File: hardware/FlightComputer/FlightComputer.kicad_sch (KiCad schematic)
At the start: 46 parts

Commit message: Add USB, Sensor Stack, Camera, TestPoints.
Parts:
- removed C? (x3): Capacitor 10nF +/-20% 50V 0402, CAPC0402(1005)60_L, symbol FCU-altium-import:0_CAP-NP-2
- removed C?: Capacitor 10nF +/-20% 50V 0402, CAPC0402(1005)60_L, symbol FCU-altium-import:2_CAP-NP-2
- removed C?: Capacitor 1µF +/-0.1% 25V 0603, CAPC0603(1608)100_L, symbol FCU-altium-import:3_CAP-NP-2
- removed C? (x2): Capacitor, symbol FCU-altium-import:1_Capacitor
- added C? (x2): 10n, symbol Device:C_Small
- added C? (x2): 22n, symbol Device:C_Small
- added C? (x2): 100n, symbol Device:C_Small
- added C?: 1u, symbol Device:C_Small
- added J?: Mag, Connector_PinSocket_2.54mm:PinSocket_1x09_P2.54mm_Vertical, symbol Connector:Conn_01x09_Female
- added J?: Camera, symbol Connector:Conn_01x08_Female
- added J?: IMU, symbol Connector:Conn_01x05_Female
- added J?: USB_B_Micro, symbol Connector:USB_B_Micro
- added R? (x3): 4k7, symbol Device:R_Small
- added R? (x2): 20, symbol Device:R_Small
- added TP? (x15): TestPoint, symbol Connector:TestPoint
- added U? (x3): LM75AD, symbol LM75A:SO8
- added U?: USBLC6-2SC6, Package_TO_SOT_SMD:SOT-23-6, symbol Power_Protection:USBLC6-2SC6
- J?: value Conn_02x05_Odd_Even -> SWD
- R?: ALTIUM_VALUE 162K -> 162k
- R?: value pick one -> 1k
- R?: ALTIUM_VALUE 133K -> 133k
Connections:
- net +3V3: now also R?.1, R?.1, TP?.1
- net +5V: now also C?.1, C?.1, TP?.1
- net EN1: now also TP?.1
- net EN2: now also TP?.1
- net GND: now also C?.2, C?.2, C?.2, J?.2 (Pin_2), J?.2 (Pin_2), J?.4 (ID), J?.5 (GND), J?.5 (Pin_5), J?.7 (Pin_7), TP?.1, U?.2 (GND), U?.4 (GND), U?.4 (GND), U?.4 (GND), U?.5 (A2), U?.5 (A2), U?.6 (A1)
- net GNDA: now also C?.1, C?.2, TP?.1
- net I2C1_SCL: now also R?.2, J?.4 (Pin_4), J?.8 (Pin_8), TP?.1, U?.2 (SCL), U?.2 (SCL), U?.2 (SCL); no longer R?.2
- net I2C1_SDA: now also R?.2, J?.3 (Pin_3), J?.7 (Pin_7), TP?.1, U?.1 (SDA), U?.1 (SDA), U?.1 (SDA); no longer R?.2
- net I2C2_SCL: now also R?.2, TP?.1
- net I2C2_SDA: now also R?.2, TP?.1
- net LED_STATUS: now also U?.51 (PB12); no longer U?.46 (PE15)
- net SPI1_MISO: now also J?.3 (Pin_3), J?.5 (Pin_5), TP?.1
- net SPI1_MOSI: now also J?.2 (Pin_2), J?.4 (Pin_4), TP?.1
- net SPI1_SCK: now also J?.3 (Pin_3), J?.4 (Pin_4), TP?.1
- net USB_D+: now also U?.4 (I/O2)
- net USB_D-: now also U?.6 (I/O1)
- net at IC?.15 (VBST2): now also C?.1
- net at IC?.14 (SW2), L?.1: now also C?.2
- net at IC?.6 (SS1): now also C?.2
- net at IC?.2 (VBST1): now also C?.2
- net at IC?.3 (SW1), L?.2: now also C?.1
- net at IC?.9 (VREG5): now also C?.1
- net CS2: now reaches U?.23 (PA0)
- net CS2: now also J?.6 (Pin_6), TP?.1
- net CS1: now reaches U?.67 (PA8)
- net CS1: now also J?.1 (Pin_1), TP?.1
- net at IC?.11 (SS2): now also C?.1
- new net: J?.3 (D+), R?.1, R?.2
- new net: J?.2 (D-), R?.2
- new net +3.3V: J?.1 (Pin_1), J?.1 (Pin_1), J?.6 (Pin_6), U?.5 (A2), U?.6 (A1), U?.6 (A1), U?.7 (A0), U?.7 (A0), U?.7 (A0), U?.8 (VCC), U?.8 (VCC), U?.8 (VCC)
- new net +5VD: J?.1 (VBUS), R?.1, U?.5 (VBUS)
- new net PE15: U?.46 (PE15)
- new net USB_CONN_D+: R?.2, U?.3 (I/O2)
- new net USB_CONN_D-: R?.1, U?.1 (I/O1)
- no-connect marks 2 -> 9
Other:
- note added: "I2C Devices"
- note added: "Power Conditioning"
- note added: "Rail Creation"
- note added: "SPI Devices"
- note added: "Serial Wire Debug"
- note added: "USB"
- note added: "X OSC"
- moved on the sheet: C?, D?, J?, L?, R?, SW?, U?, Y?

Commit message: Add Annotations
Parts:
- gave numbers to parts that had none: 74

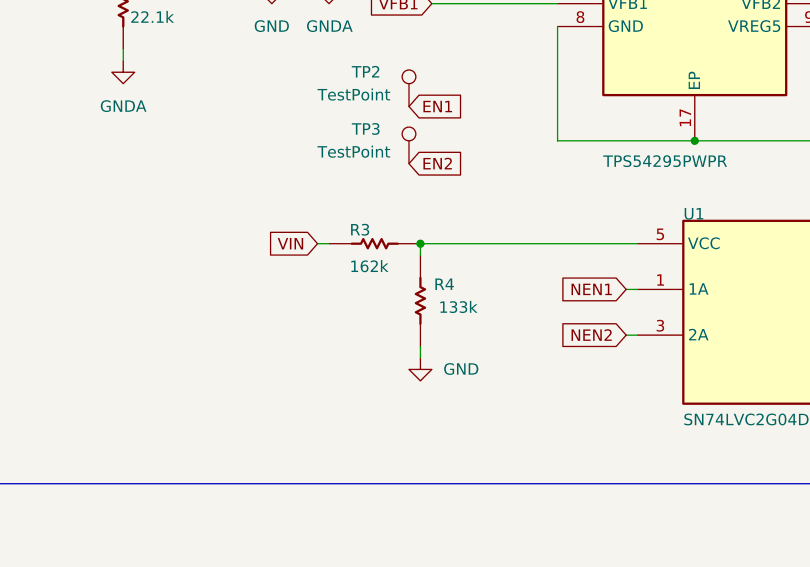
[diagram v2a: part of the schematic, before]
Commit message: Migrate some altium stuff to KiCad version
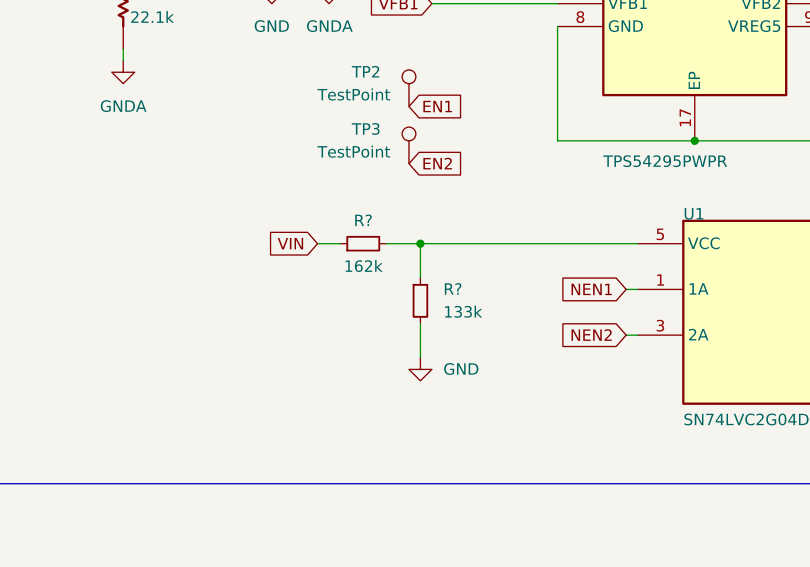
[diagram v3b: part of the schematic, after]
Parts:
- removed R3: Resistor, symbol FCU-altium-import:2_Resistor
- removed R4: Resistor, symbol FCU-altium-import:3_Resistor
- added R?: 133k, symbol Device:R_Small
- added R?: 162k, symbol Device:R_Small
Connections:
- net GND: now also R?.2
- net VIN: now also R?.1
- net at U1.5 (VCC): now also R?.1, R?.2
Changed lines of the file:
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@@
   (junction (at 379.73 119.38) (diameter 0) (color 0 0 0 0)
   )
-  (junction (at 73.66 120.65) (diameter 0) (color 0 0 0 0)
-  )
   (junction (at 156.21 76.2) (diameter 0) (color 0 0 0 0)
   )
@@
   (junction (at 379.73 116.84) (diameter 0) (color 0 0 0 0)
   )
-  (junction (at 254 76.2) (diameter 0) (color 0 0 0 0)
-  )
   (junction (at 40.64 76.2) (diameter 0) (color 0 0 0 0)
   )
+  (junction (at 254 76.2) (diameter 0) (color 0 0 0 0)
+  )
   (junction (at 379.73 157.48) (diameter 0) (color 0 0 0 0)
   )
@@
   (junction (at 152.4 76.2) (diameter 0) (color 0 0 0 0)
   )
+  (junction (at 73.66 120.65) (diameter 0) (color 0 0 0 0)
+  )
   (junction (at 88.9 68.58) (diameter 0) (color 0 0 0 0)
   )
@@
     (stroke (width 0) (type default) (color 0 0 0 0))
   )
-  (wire (pts (xy 62.23 120.65) (xy 63.5 120.65))
+  (wire (pts (xy 62.23 120.65) (xy 64.77 120.65))
     (stroke (width 0) (type default) (color 0 0 0 0))
   )
@@
     (stroke (width 0) (type default) (color 0 0 0 0))
   )
+  (wire (pts (xy 254 76.2) (xy 256.54 76.2))
+    (stroke (width 0) (type default) (color 0 0 0 0))
+  )
   (wire (pts (xy 328.93 187.96) (xy 328.93 193.04))
     (stroke (width 0) (type default) (color 0 0 0 0))
@@
     (stroke (width 0) (type default) (color 0 0 0 0))
   )
-  (wire (pts (xy 73.66 133.35) (xy 73.66 132.08))
+  (wire (pts (xy 73.66 129.54) (xy 73.66 133.35))
     (stroke (width 0) (type default) (color 0 0 0 0))
   )
@@
     (stroke (width 0) (type default) (color 0 0 0 0))
   )
-  (wire (pts (xy 73.66 121.92) (xy 73.66 120.65))
+  (wire (pts (xy 73.66 120.65) (xy 73.66 124.46))
     (stroke (width 0) (type default) (color 0 0 0 0))
   )
@@
     (stroke (width 0) (type default) (color 0 0 0 0))
   )
+  (wire (pts (xy 69.85 120.65) (xy 73.66 120.65))
+    (stroke (width 0) (type default) (color 0 0 0 0))
+  )
   (wire (pts (xy 166.37 86.36) (xy 166.37 88.9))
     (stroke (width 0.254) (type default) (color 0 0 0 0))
@@
     (stroke (width 0.254) (type default) (color 0 0 0 0))
   )
-  (wire (pts (xy 254 76.2) (xy 256.54 76.2))
-    (stroke (width 0) (type default) (color 0 0 0 0))
-  )
   (wire (pts (xy 323.85 111.76) (xy 330.2 111.76))
     (stroke (width 0) (type default) (color 0 0 0 0))
@@
     (pin "2")
   )
-  (symbol (lib_id "FCU-altium-import:2_Resistor") (at 73.66 120.65 0) (unit 1)
-    (in_bom yes) (on_board yes)
-    (property "Reference" "R3" (id 0) (at 65.786 119.888 0)
-      (effects (font (size 1.27 1.27)) (justify left bottom))
-    )
-    (property "Value" "Resistor" (id 1) (at 62.992 119.888 0)
-      (effects (font (size 1.27 1.27)) (justify left bottom) hide)
-    )
-    (property "Footprint" "" (id 2) (at 73.66 120.65 0)
-      (effects (font (size 1.27 1.27)) hide)
-    )
-    (property "Datasheet" "" (id 3) (at 73.66 120.65 0)
-      (effects (font (size 1.27 1.27)) hide)
-    )
-    (property "DTEMP" "" (id 4) (at 62.992 119.888 0)
-      (effects (font (size 1.27 1.27)) (justify left bottom) hide)
-    )
-    (property "T_REL_LOCAL" "" (id 5) (at 62.992 119.888 0)
-      (effects (font (size 1.27 1.27)) (justify left bottom) hide)
-    )
-    (property "TC" "" (id 6) (at 62.992 119.888 0)
-      (effects (font (size 1.27 1.27)) (justify left bottom) hide)
-    )
-    (property "TC1" "0" (id 7) (at 62.992 119.888 0)
-      (effects (font (size 1.27 1.27)) (justify left bottom) hide)
-    )
-    (property "TC2" "0" (id 8) (at 62.992 119.888 0)
-      (effects (font (size 1.27 1.27)) (justify left bottom) hide)
-    )
-    (property "TEMP" "" (id 9) (at 62.992 119.888 0)
-      (effects (font (size 1.27 1.27)) (justify left bottom) hide)
-    )
-    (property "SIMULATIONGENERICCOMPONENT" "True" (id 10) (at 62.992 119.888 0)
-      (effects (font (size 1.27 1.27)) (justify left bottom) hide)
-    )
-    (property "ALTIUM_VALUE" "162k" (id 11) (at 65.786 123.952 0)
-      (effects (font (size 1.27 1.27)) (justify left bottom))
-    )
-    (pin "1")
-    (pin "2")
-  )
   (symbol (lib_id "power:GND") (at 361.95 143.51 0) (unit 1)
     (in_bom yes) (on_board yes) (fields_autoplaced)
@@
     (pin "8")
   )
+  (symbol (lib_id "Device:R_Small") (at 73.66 127 0) (unit 1)
+    (in_bom yes) (on_board yes) (fields_autoplaced)
+    (property "Reference" "R?" (id 0) (at 76.2 125.7299 0)
+      (effects (font (size 1.27 1.27)) (justify left))
+    )
+    (property "Value" "133k" (id 1) (at 76.2 128.2699 0)
+      (effects (font (size 1.27 1.27)) (justify left))
+    )
+    (property "Footprint" "" (id 2) (at 73.66 127 0)
+      (effects (font (size 1.27 1.27)) hide)
+    )
+    (property "Datasheet" "~" (id 3) (at 73.66 127 0)
+      (effects (font (size 1.27 1.27)) hide)
+    )
+    (pin "1")
+    (pin "2")
+  )
   (symbol (lib_id "power:+3.3VA") (at 201.93 92.71 0) (unit 1)
     (in_bom yes) (on_board yes) (fields_autoplaced)
@@
     (pin "1")
   )
-  (symbol (lib_id "FCU-altium-import:3_Resistor") (at 73.66 132.08 180) (unit 1)
-    (in_bom yes) (on_board yes)
-    (property "Reference" "R4" (id 0) (at 77.47 124.46 0)
-      (effects (font (size 1.27 1.27)) (justify left bottom))
-    )
-    (property "Value" "Resistor" (id 1) (at 74.422 132.588 0)
-      (effects (font (size 1.27 1.27)) (justify left bottom) hide)
-    )
-    (property "Footprint" "" (id 2) (at 73.66 132.08 0)
-      (effects (font (size 1.27 1.27)) hide)
-    )
-    (property "Datasheet" "" (id 3) (at 73.66 132.08 0)
-      (effects (font (size 1.27 1.27)) hide)
-    )
-    (property "DTEMP" "" (id 4) (at 74.422 132.588 0)
-      (effects (font (size 1.27 1.27)) (justify left bottom) hide)
-    )
-    (property "T_REL_LOCAL" "" (id 5) (at 74.422 132.588 0)
-      (effects (font (size 1.27 1.27)) (justify left bottom) hide)
-    )
-    (property "TC" "" (id 6) (at 74.422 132.588 0)
-      (effects (font (size 1.27 1.27)) (justify left bottom) hide)
-    )
-    (property "TC1" "0" (id 7) (at 74.422 132.588 0)
-      (effects (font (size 1.27 1.27)) (justify left bottom) hide)
-    )
-    (property "TC2" "0" (id 8) (at 74.422 132.588 0)
-      (effects (font (size 1.27 1.27)) (justify left bottom) hide)
-    )
-    (property "TEMP" "" (id 9) (at 74.422 132.588 0)
-      (effects (font (size 1.27 1.27)) (justify left bottom) hide)
-    )
-    (property "SIMULATIONGENERICCOMPONENT" "True" (id 10) (at 74.422 132.588 0)
-      (effects (font (size 1.27 1.27)) (justify left bottom) hide)
-    )
-    (property "ALTIUM_VALUE" "133k" (id 11) (at 80.01 127 0)
-      (effects (font (size 1.27 1.27)) (justify left bottom))
-    )
-    (pin "1")
-    (pin "2")
-  )
   (symbol (lib_id "power:+3.3V") (at 367.03 87.63 0) (unit 1)
     (in_bom yes) (on_board yes) (fields_autoplaced)
@@
     (pin "1")
   )
+  (symbol (lib_id "Device:R_Small") (at 67.31 120.65 90) (unit 1)
+    (in_bom yes) (on_board yes)
+    (property "Reference" "R?" (id 0) (at 67.31 118.11 90))
+    (property "Value" "162k" (id 1) (at 67.31 123.19 90))
+    (property "Footprint" "" (id 2) (at 67.31 120.65 0)
+      (effects (font (size 1.27 1.27)) hide)
+    )
+    (property "Datasheet" "~" (id 3) (at 67.31 120.65 0)
+      (effects (font (size 1.27 1.27)) hide)
+    )
+    (pin "1")
+    (pin "2")
+  )
   (symbol (lib_id "power:GND") (at 321.31 107.95 180) (unit 1)
     (in_bom yes) (on_board yes) (fields_autoplaced)
@@
       (reference "R2") (unit 1) (value "Resistor") (footprint "")
     )
-    (path "/19a35de1-7694-4787-a2ca-1d53553f76ff"
-      (reference "R3") (unit 1) (value "Resistor") (footprint "")
-    )
-    (path "/67bb5a90-0d4f-47d5-af25-0b2e4f4b8844"
-      (reference "R4") (unit 1) (value "Resistor") (footprint "")
-    )
     (path "/b9b3c0af-f53a-4ed9-bc6a-86ba05adcef9"
       (reference "R5") (unit 1) (value "Resistor") (footprint "")
@@
       (reference "R16") (unit 1) (value "20") (footprint "")
     )
+    (path "/3ea5b68e-e3c6-48b5-bbec-20f864d5adfd"
+      (reference "R?") (unit 1) (value "133k") (footprint "")
+    )
+    (path "/ac546c15-b25b-4893-b7f0-0c0875eafca7"
+      (reference "R?") (unit 1) (value "162k") (footprint "")
+    )
     (path "/bed40b41-5999-4bc9-a63c-895afedb7651"

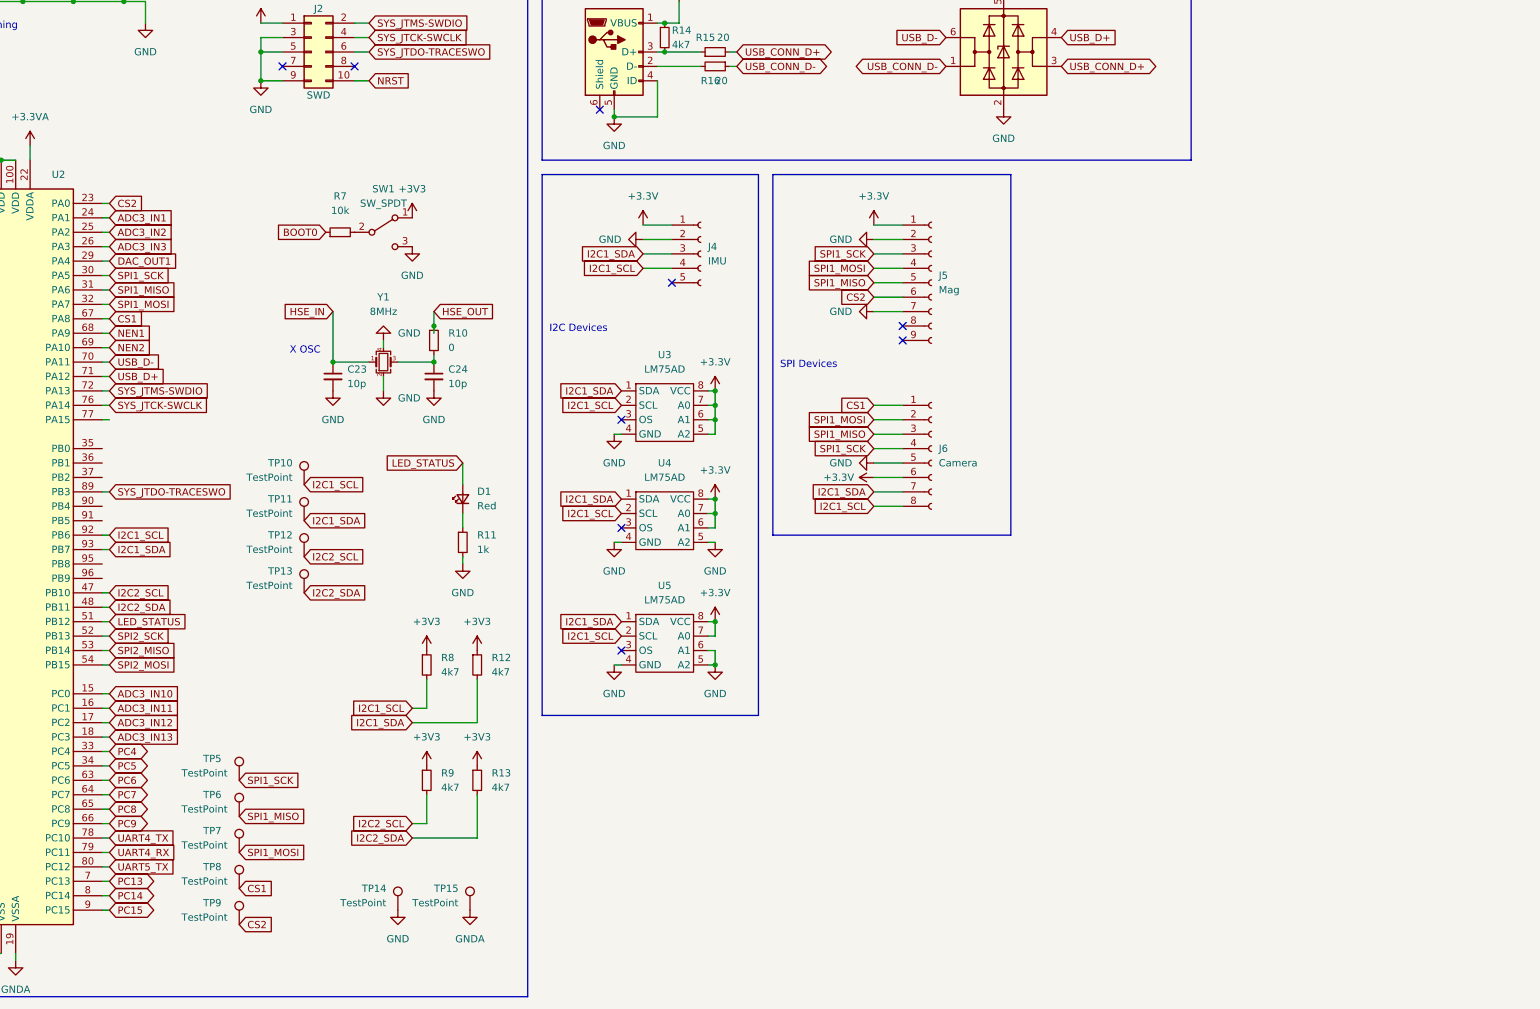
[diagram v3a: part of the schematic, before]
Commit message: add 15pin dsub
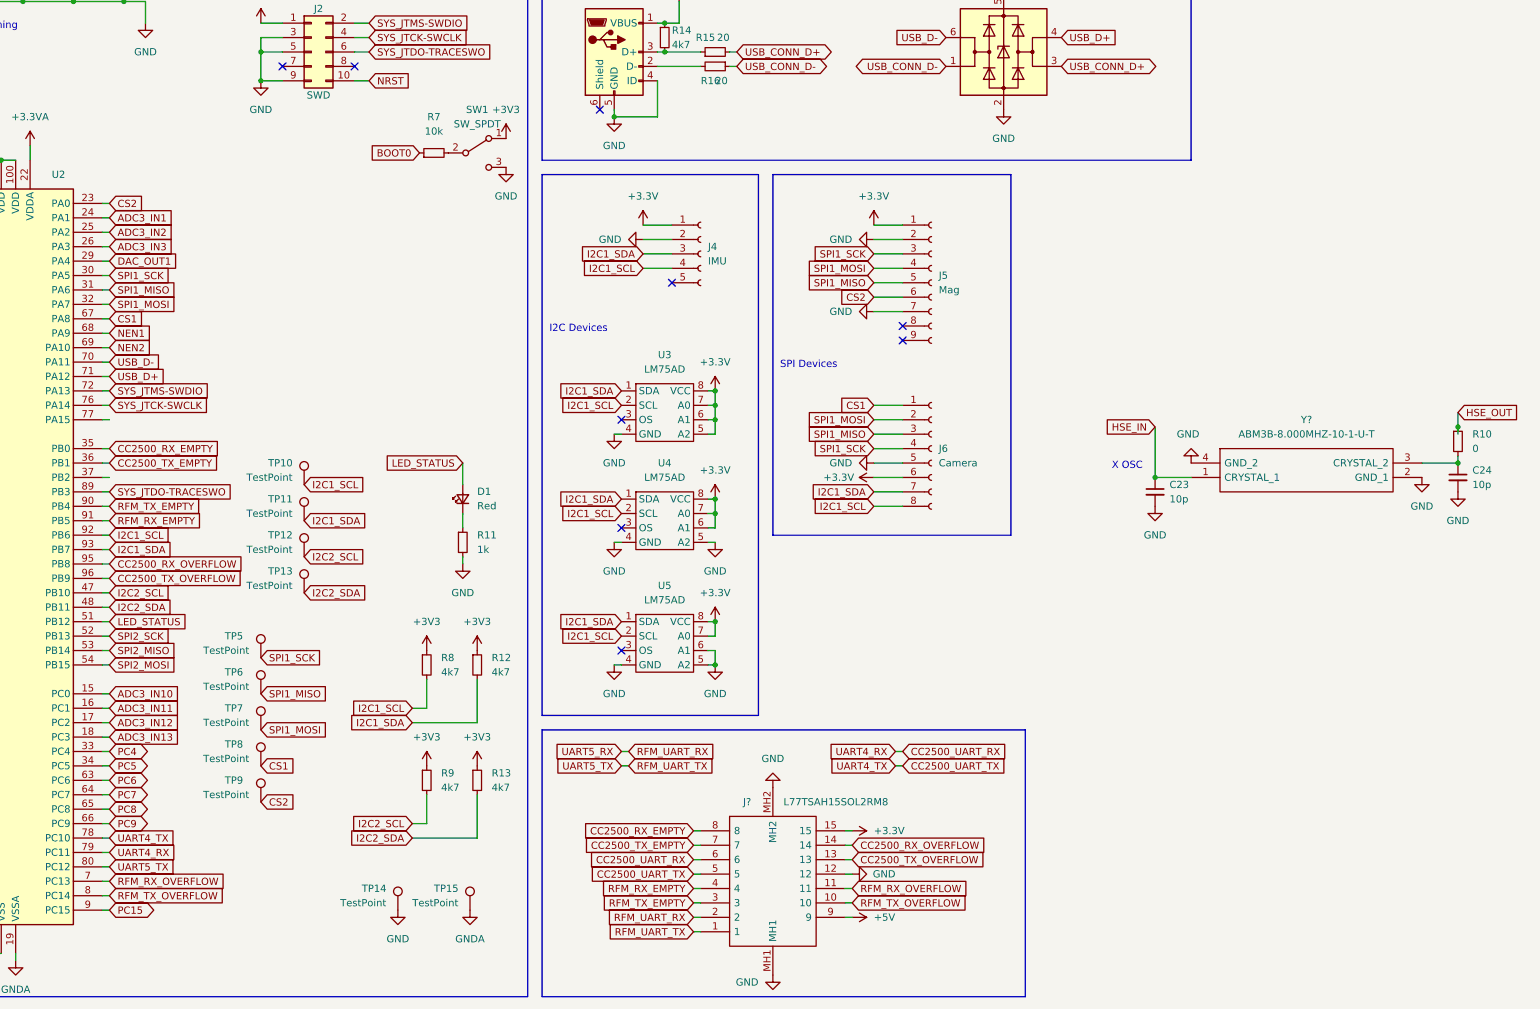
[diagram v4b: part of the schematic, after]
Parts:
- removed Y1: 8MHz, symbol Device:Crystal_GND24_Small
- added J?: L77TSAH15SOL2RM8, L77TSAH15SOL2RM8, symbol SamacSys_Parts:L77TSAH15SOL2RM8
- added Y?: ABM3B-8.000MHZ-10-1-U-T, ABM3B, symbol SamacSys_Parts:ABM3B-8.000MHZ-10-1-U-T
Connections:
- net +3.3V: now also J?.15
- net +5V: now also J?.9
- net GND: now also J?.12, J?.MH1, J?.MH2, Y?.2 (GND_1), Y?.4 (GND_2)
- net HSE_IN: now also Y?.1 (CRYSTAL_1)
- net at C24.1, R10.2: now also Y?.3 (CRYSTAL_2)
- net CC2500_RX_EMPTY: now reaches U2.35 (PB0)
- net CC2500_RX_EMPTY: now also J?.8
- net CC2500_TX_EMPTY: now reaches U2.36 (PB1)
- net CC2500_TX_EMPTY: now also J?.7
- net RFM_TX_EMPTY: now reaches U2.90 (PB4)
- net RFM_TX_EMPTY: now also J?.3
- net RFM_RX_EMPTY: now reaches U2.91 (PB5)
- net RFM_RX_EMPTY: now also J?.4
- net CC2500_RX_OVERFLOW: now reaches U2.95 (PB8)
- net CC2500_RX_OVERFLOW: now also J?.14
- net CC2500_TX_OVERFLOW: now reaches U2.96 (PB9)
- net CC2500_TX_OVERFLOW: now also J?.13
- net PC13 renamed RFM_RX_OVERFLOW
- net RFM_RX_OVERFLOW: now also J?.11
- net PC14 renamed RFM_TX_OVERFLOW
- net RFM_TX_OVERFLOW: now also J?.10
- net UART4_RX renamed CC2500_UART_RX
- net CC2500_UART_RX: now also J?.6
- net UART4_TX renamed CC2500_UART_TX
- net CC2500_UART_TX: now also J?.5
- net UART5_RX renamed RFM_UART_RX
- net RFM_UART_RX: now also J?.2
- net UART5_TX renamed RFM_UART_TX
- net RFM_UART_TX: now also J?.1
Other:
- moved on the sheet: C23, C24, R10, R7, SW1, TP5, TP6, TP7, TP8, TP9
